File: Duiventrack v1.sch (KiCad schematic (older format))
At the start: 20 parts, among them P1 CONN_01X06, U1 MCP1711-SOT23-5, U2 SP-ABZ-G

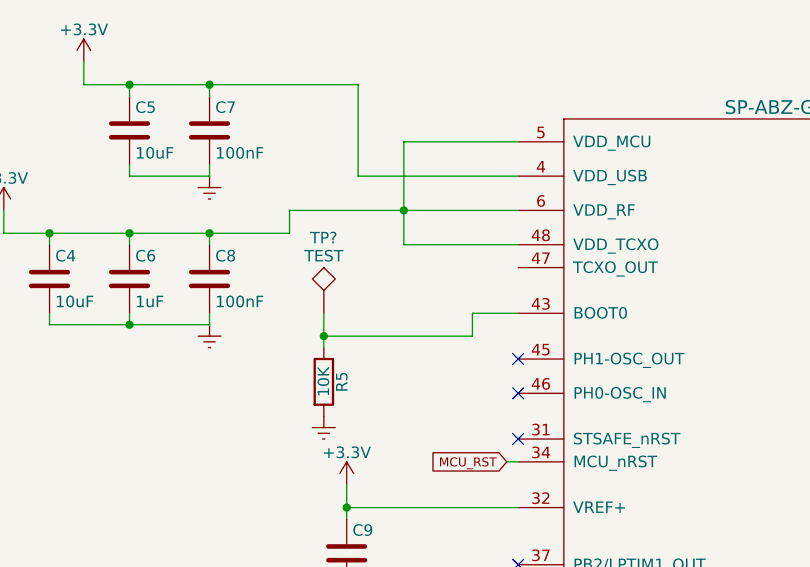
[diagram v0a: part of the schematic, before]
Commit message: Revert "Add test point - boot-0"
This reverts commit 833b218a88f86450883f1825dc2b70f2262aafe3.
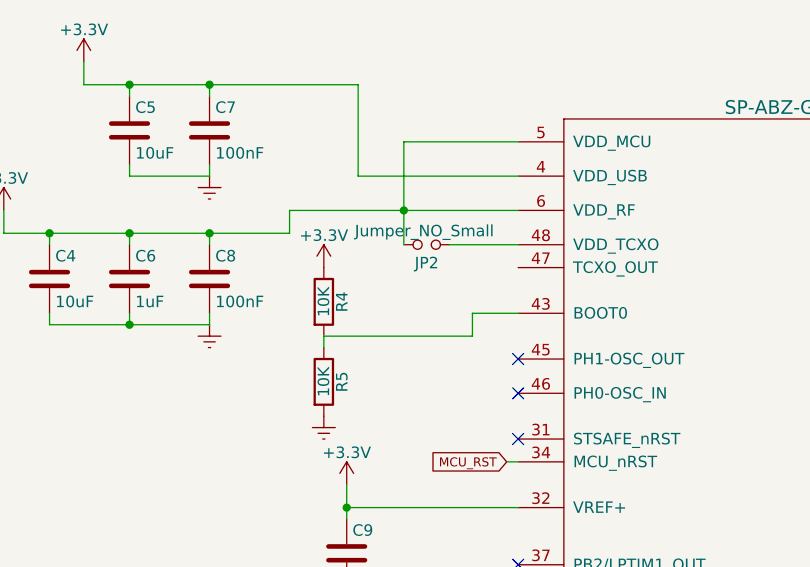
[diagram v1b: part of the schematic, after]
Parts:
- removed TP?: TEST, symbol TEST
- added JP2: Jumper_NO_Small, Footprint:SolderJumper_NO, symbol Jumper_NO_Small
- added R4: 10K, Resistors_SMD:R_0402, symbol R
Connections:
- net +3V3: now also JP2.2, R4.1; no longer U2.48 (VDD_TCXO)
- net at R5.1, U2.43 (BOOT0): now also R4.2
- new net: JP2.1, U2.48 (VDD_TCXO)
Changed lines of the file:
@@
+$EndComp
+$Comp
+L R R4
+U 1 1 5AD740C0
+P 7200 2050
+F 0 "R4" V 7280 2050 50  0000 C CNN
+F 1 "10K" V 7200 2050 50  0000 C CNN
+F 2 "Resistors_SMD:R_0402" V 7130 2050 50  0001 C CNN
+F 3 "" H 7200 2050 50  0000 C CNN
+	1    7200 2050
+	1    0    0    -1
+$EndComp
+$Comp
+L +3.3V #PWR015
+U 1 1 5AD74B56
+P 7200 1900
+F 0 "#PWR015" H 7200 1750 50  0001 C CNN
+F 1 "+3.3V" H 7200 2040 50  0000 C CNN
+F 2 "" H 7200 1900 50  0000 C CNN
+F 3 "" H 7200 1900 50  0000 C CNN
+	1    7200 1900
+	1    0    0    -1
 $EndComp
 $Comp
@@
 	7200 2200 7850 2200
 Wire Wire Line
-	7200 2100 7200 2250
+	7200 2250 7200 2200
 Wire Wire Line
 	3900 1450 3900 1400
@@
 Connection ~ 7550 1650
 Wire Wire Line
-	7550 1800 8050 1800
+	7750 1800 8050 1800
 $Comp
 L C C2
@@
 Wire Wire Line
 	3700 4400 3750 4400
+$Comp
+L Jumper_NO_Small JP2
+U 1 1 5AD7946A
+P 7650 1800
+F 0 "JP2" H 7650 1880 50  0000 C CNN
+F 1 "Jumper_NO_Small" H 7660 1740 50  0000 C CNN
+F 2 "Footprint:SolderJumper_NO" H 7650 1800 50  0001 C CNN
+F 3 "" H 7650 1800 50  0000 C CNN
+	1    7650 1800
+	-1   0    0    1
+$EndComp
 NoConn ~ 10250 1350
 NoConn ~ 10250 1500
@@
 NoConn ~ 8050 2450
 NoConn ~ 8050 2650
-$Comp
-L TEST TP?
-U 1 1 5AE0751B
-P 7200 2100
-F 0 "TP?" H 7200 2400 50  0000 C BNN
-F 1 "TEST" H 7200 2350 50  0000 C CNN
-F 2 "" H 7200 2100 50  0001 C CNN
-F 3 "" H 7200 2100 50  0001 C CNN
-	1    7200 2100
-	1    0    0    -1
-$EndComp
-Connection ~ 7200 2200
 $EndSCHEMATC
